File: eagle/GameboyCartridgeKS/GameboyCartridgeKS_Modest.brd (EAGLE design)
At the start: 49.3 x 48 mm, 36 parts, among them IC2 MEGA64-A, Y1 16MHz max

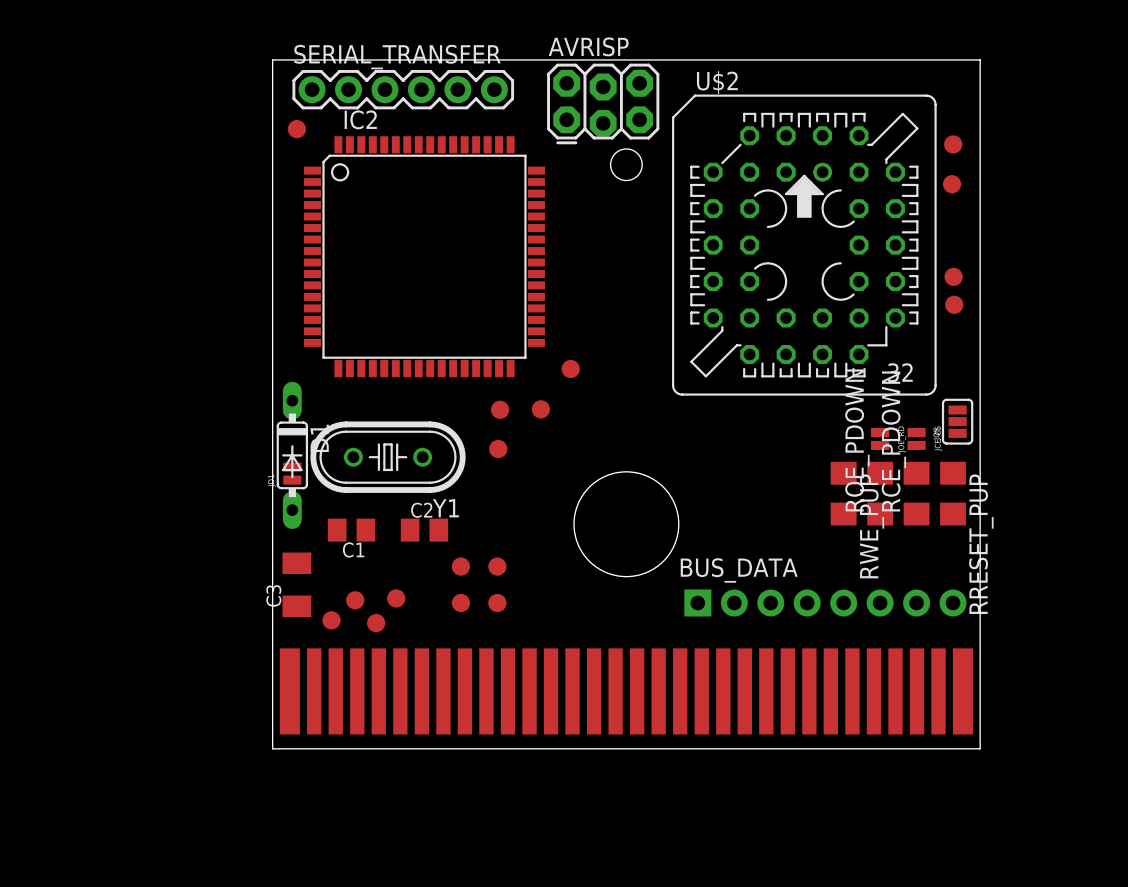
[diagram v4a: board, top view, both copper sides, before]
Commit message: Sent v1.0 MODEST to production
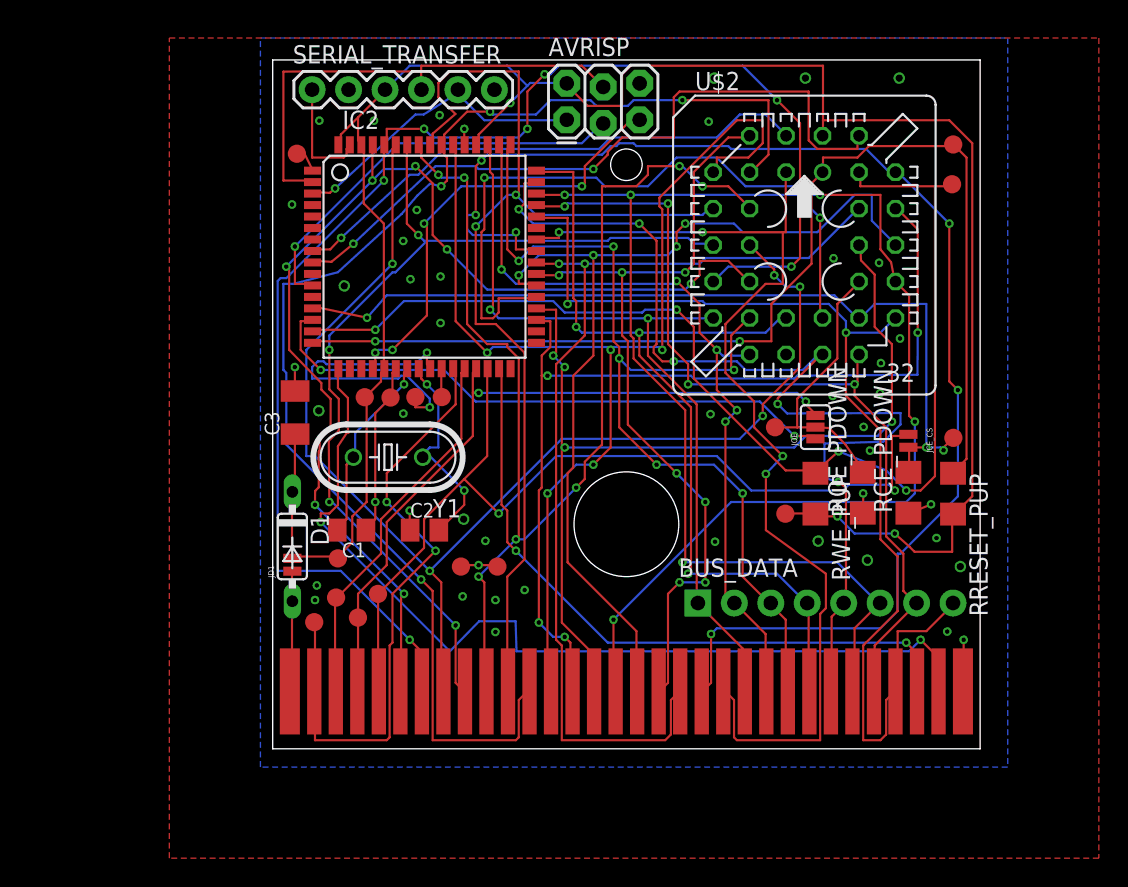
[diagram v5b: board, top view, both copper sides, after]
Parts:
- removed JOE_RD: (no value), SparkFun-Passives:PAD-JUMPER-2-NO_NO_SILK
- added U$3: (no value), kalshagar-images:GAMEBOY_LOGO
- moved PEN4 21.0 mm to (36.6, 16.4)
- moved TP2 16.3 mm to (35.9, 22.4)
- moved TP5 14.5 mm to (7.27, 24.5)
- moved C3 12.0 mm to (2.41, 23.4)
- moved TP6 10.5 mm to (9.06, 24.5)
- moved JOE 9.91 mm to (38.7, 22.4)
- moved TP1 9.27 mm to (48.3, 21.7)
- moved PEN3 9.12 mm to (5.40, 13.3)
- moved SCL 6.82 mm to (10.8, 24.5)
- moved D1 6.35 mm to (2.22, 14.1)
- moved JD1 6.35 mm to (2.22, 12.8)
- moved SDA 4.16 mm to (12.6, 24.5)
- moved RWE_PUP 1.97 mm to (38.7, 17.8)
- moved PEN 1.71 mm to (2.54, 41.5)
- moved SCL2 1.35 mm to (5.27, 10.5)
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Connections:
- net N$1 renamed SDA
- net N$5 renamed SCL
- net !GB_RD: no longer JOE_RD.1
- net !OE: no longer JOE_RD.2
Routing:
- net VCC: track 0.00 -> 149.1 mm, vias 0 -> 3
- net ADDRESS1: track 0.00 -> 99.8 mm, vias 0 -> 7
- net ADDRESS10: track 0.00 -> 96.2 mm, vias 0 -> 4
- net ADDRESS14: track 0.05 -> 94.4 mm, vias 0 -> 6
- net ADDRESS6: track 0.00 -> 93.1 mm, vias 0 -> 4
- net ADDRESS2: track 0.00 -> 87.8 mm, vias 0 -> 5
- net ADDRESS4: track 0.00 -> 84.2 mm, vias 0 -> 7
- net ADDRESS7: track 0.00 -> 81.1 mm, vias 0 -> 5
- net !WE: track 0.00 -> 81.0 mm, vias 0 -> 4
- net !RESET: track 0.00 -> 79.4 mm, vias 0 -> 2
- net ADDRESS0: track 0.00 -> 79.4 mm, vias 0 -> 7
- net 29: track 0.05 -> 77.9 mm, vias 0 -> 2
- net 27: track 0.00 -> 76.8 mm, vias 0 -> 4
- net ADDRESS15: track 0.00 -> 73.9 mm, vias 0 -> 4
- net ADDRESS5: track 0.05 -> 73.7 mm, vias 0 -> 2
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- added copper zone on layer 1, net GND
- added copper zone on layer 16, net GND
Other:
- board text added: "!CE"
- board text added: "!CE!=!CS!"
- board text added: "!CE!dn"
- board text added: "!CS"
- board text added: "!OE"
- board text added: "!OE!=!RD!"
- board text added: "!OE!=B4"
- board text added: "!OE!dn"
- board text added: "!RD"
- board text added: "!RST"
- board text added: "!RST!up"
- board text added: "!WE"
- board text added: "!WE!up"
- board text added: "!WR"
- board text added: "10uF"
- board text added: "16 MHz MAX"
- board text added: "22pF"
- board text added: "ATmega64a"
- board text added: "CLK"
- board text added: "Data bus"
- board text added: "EN29F002T"
- board text added: "GND"
- board text added: "Gameboy cartridge "Modest edition""
- board text added: "JOE"
- board text added: "PEN"
- board text added: "RX"
- board text added: "SCL"
- board text added: "SDA"
- board text added: "TX"
- board text added: "VCC"
- board text added: "Version 1.0 - Jan2015"
- board text added: "http://kalshagar.wikispaces.com/Gameboy+homebrew+cartridge"
